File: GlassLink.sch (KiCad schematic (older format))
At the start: 37 parts, among them J1 USB_C_Receptacle_USB2.0, J2 FTSH-105-01-F-DV-K, SW1 SW_Push, U1 SN65220, U2 AP2204K-3.3, U3 LPC11U35FHI33_501, Y1 ECS-120-20-30B-TR

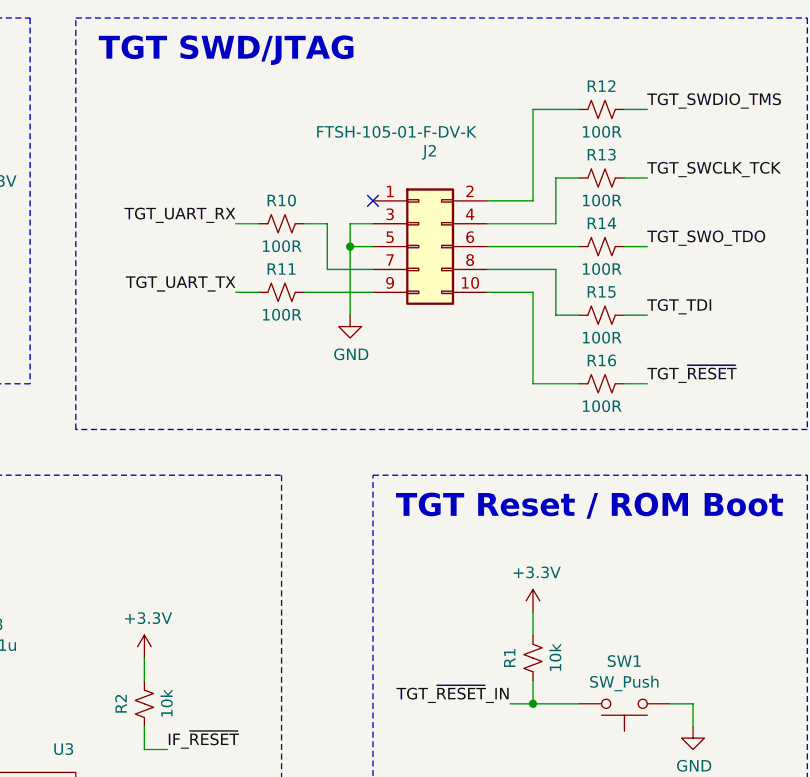
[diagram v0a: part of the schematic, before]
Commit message: Pull TGT Reset to the TGT VCC instead of the prog VCC
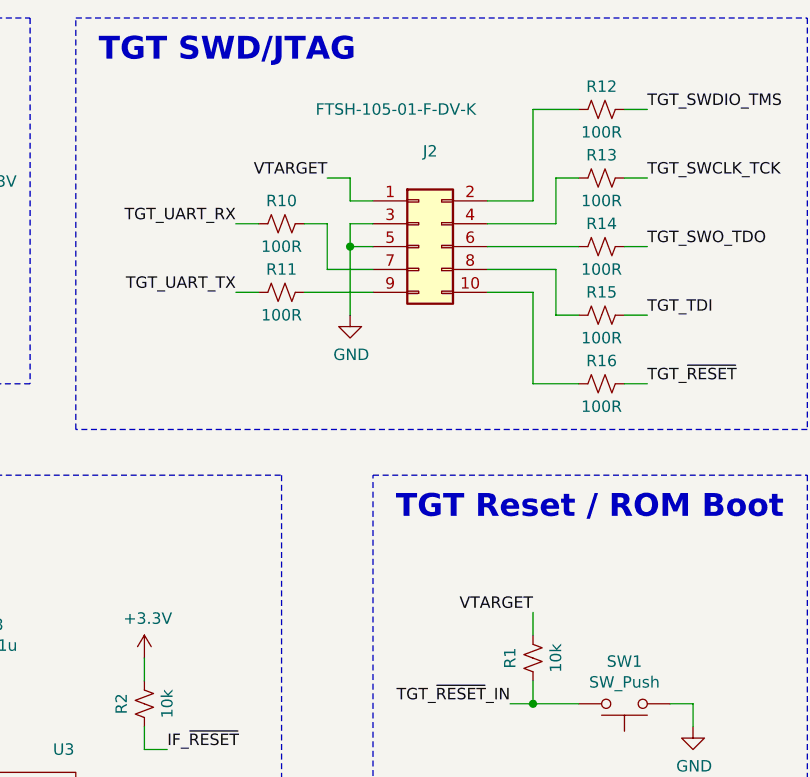
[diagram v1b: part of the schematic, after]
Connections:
- net +3V3: no longer R1.1
- net VTARGET: now reaches J2.1 (Pin_1)
- net VTARGET: now also R1.1
- no-connect marks 17 -> 16
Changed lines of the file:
@@
-$EndComp
-$Comp
-L Connector_Generic:Conn_02x05_Odd_Even J2
-U 1 1 61B17CD2
-P 8600 1700
-F 0 "J2" H 8650 2117 50  0000 C CNN
-F 1 "FTSH-105-01-F-DV-K" H 8500 2200 50  0000 C CNN
-F 2 "Connector_PinHeader_1.27mm:PinHeader_2x05_P1.27mm_Vertical_SMD" H 8600 1700 50  0001 C CNN
-F 3 "~" H 8600 1700 50  0001 C CNN
-	1    8600 1700
-	1    0    0    -1
 $EndComp
 $Comp
@@
 Wire Wire Line
 	9500 2000 9600 2000
-NoConn ~ 8400 1500
 $Comp
 L Device:R_Small_US R10
@@
 F 3 "~" H 9100 3500 50  0001 C CNN
 	1    9100 3500
-	1    0    0    -1
-$EndComp
-$Comp
-L power:+3.3V #PWR0110
-U 1 1 61BDF3AC
-P 9100 3300
-F 0 "#PWR0110" H 9100 3150 50  0001 C CNN
-F 1 "+3.3V" H 9115 3473 50  0000 C CNN
-F 2 "" H 9100 3300 50  0001 C CNN
-F 3 "" H 9100 3300 50  0001 C CNN
-	1    9100 3300
 	1    0    0    -1
 $EndComp
@@
 Text Notes 1400 5300 0    100  ~ 20
 Fiducials
+$Comp
+L Connector_Generic:Conn_02x05_Odd_Even J2
+U 1 1 61B17CD2
+P 8600 1700
+F 0 "J2" H 8650 2117 50  0000 C CNN
+F 1 "FTSH-105-01-F-DV-K" H 8500 2300 50  0000 C CNN
+F 2 "Connector_PinHeader_1.27mm:PinHeader_2x05_P1.27mm_Vertical_SMD" H 8600 1700 50  0001 C CNN
+F 3 "~" H 8600 1700 50  0001 C CNN
+	1    8600 1700
+	1    0    0    -1
+$EndComp
+Wire Wire Line
+	8400 1500 8300 1500
+Text Label 8200 1400 2    50   ~ 0
+VTARGET
+Wire Wire Line
+	8300 1500 8300 1400
+Wire Wire Line
+	8300 1400 8200 1400
+Text Label 9100 3300 2    50   ~ 0
+VTARGET
 $EndSCHEMATC

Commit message: Pulling TGT_RESET to DAPLink 3.3V rail
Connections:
- net +3V3: now also R1.1
- net VTARGET: no longer R1.1
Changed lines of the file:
@@
 Wire Wire Line
 	8300 1400 8200 1400
-Text Label 9100 3300 2    50   ~ 0
-VTARGET
+$Comp
+L power:+3.3V #PWR?
+U 1 1 61E47EDF
+P 9100 3300
+F 0 "#PWR?" H 9100 3150 50  0001 C CNN
+F 1 "+3.3V" H 9115 3473 50  0000 C CNN
+F 2 "" H 9100 3300 50  0001 C CNN
+F 3 "" H 9100 3300 50  0001 C CNN
+	1    9100 3300
+	1    0    0    -1
+$EndComp
 $EndSCHEMATC
